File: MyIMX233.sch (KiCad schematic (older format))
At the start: 81 parts, among them IC1 iMX233, IC2 DDR_SDRAM_MT46_x16, J1 USB_OTG, P1 4p2, P2 1v2, P3 VDDA1v8, P4 2v5, P5 3v3, P6 1v, SW1 SWITCH_PUSHBUTTON, Y1 24Mhz

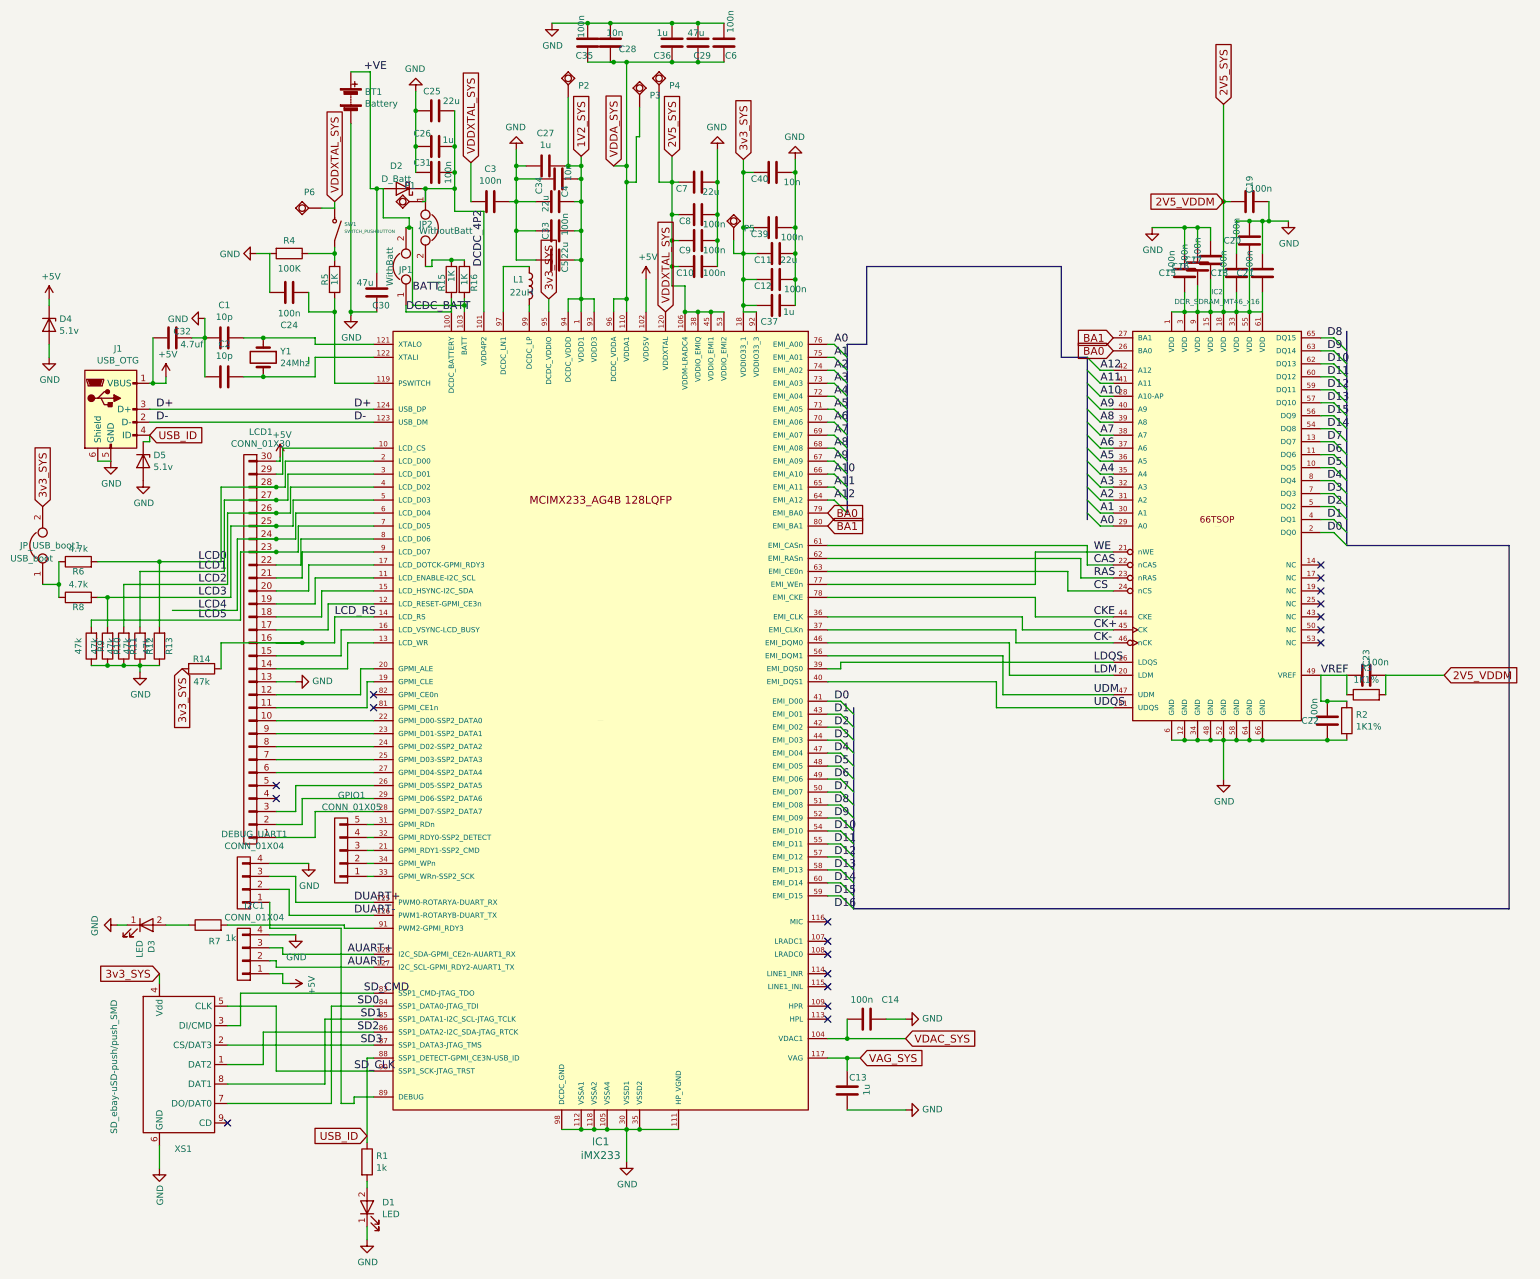
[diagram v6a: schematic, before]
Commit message: added electrolytic caps and fixed a bug in RAM CS and CE resistors
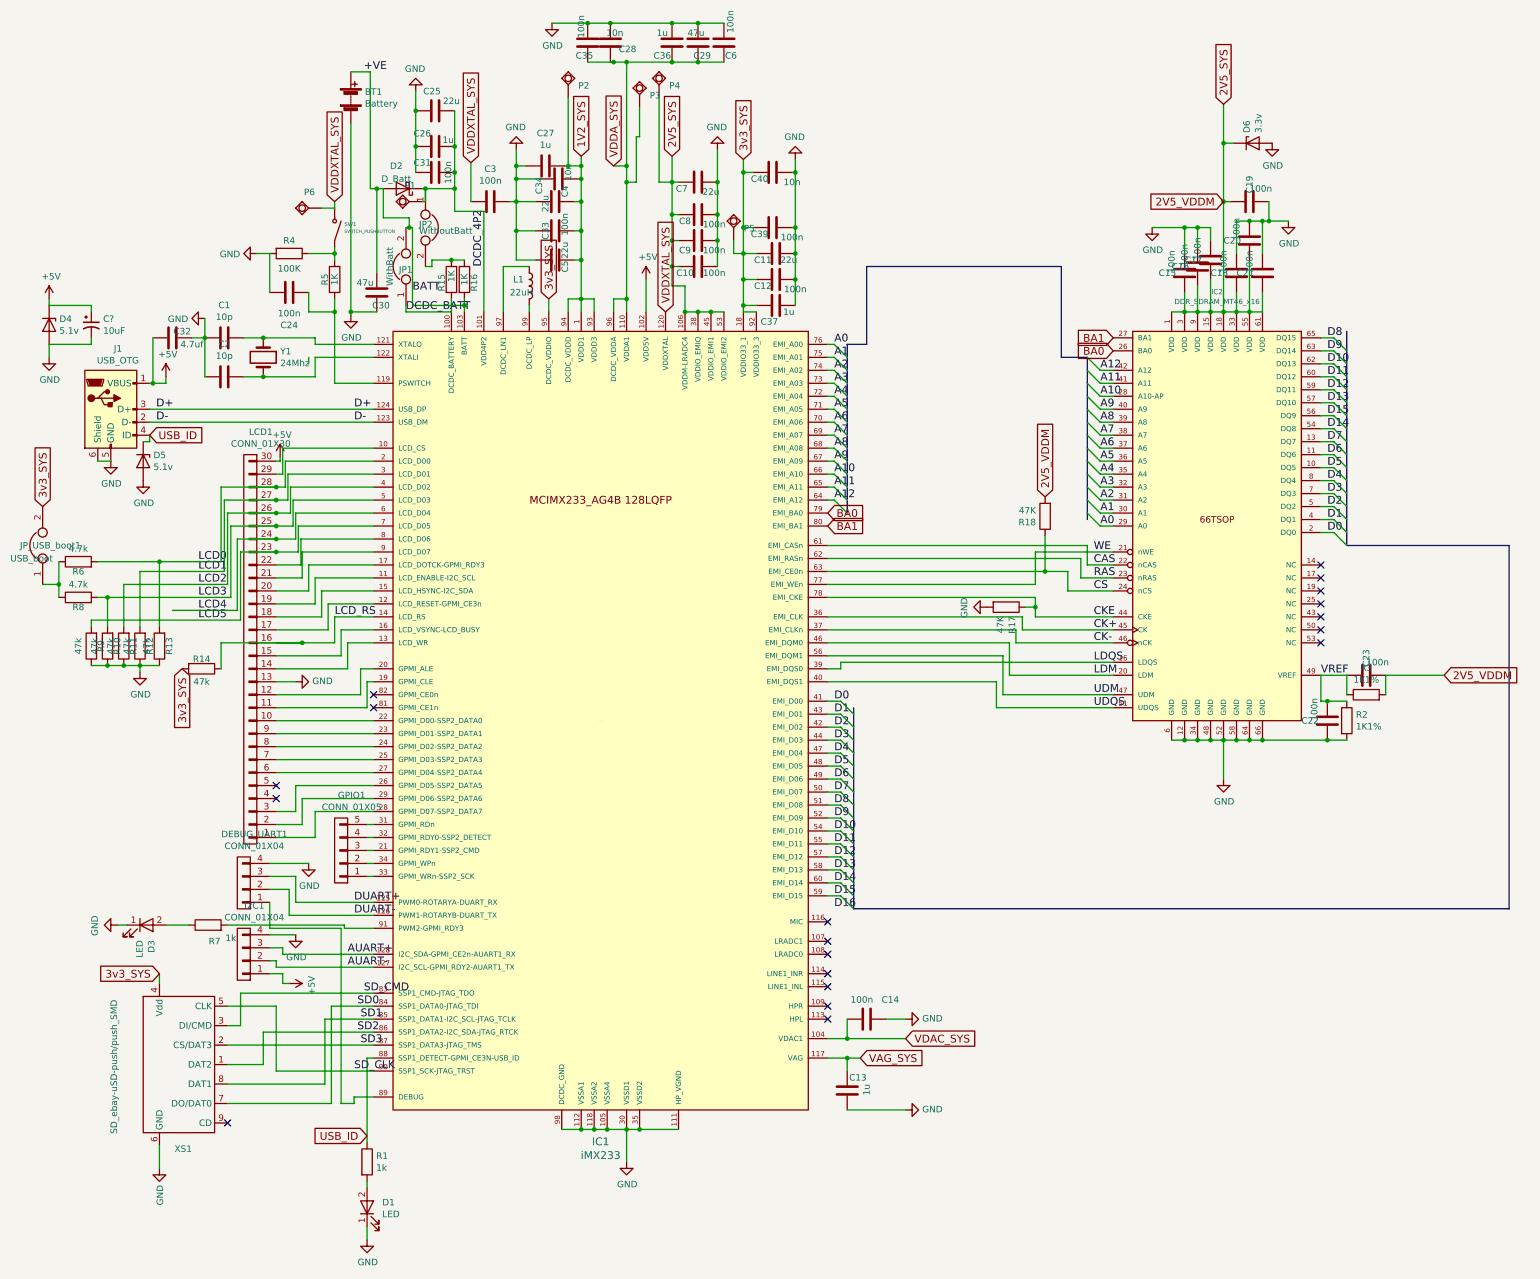
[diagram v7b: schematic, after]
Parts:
- added C?: 10uF, symbol CP1_Small
- added D6: 3.3v, Diodes_SMD:D_SOD-123, symbol D_Zener
- added R17, R18: 47K, Resistors_SMD:R_0603, symbol R
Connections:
- net +5V: now also C?.1
- net 2V5_SYS: now also D6.1 (K), R18.2
- net CKE: now also R17.1
- net CS: now also R18.1
- net GND: now also C?.2, D6.2 (A), R17.2
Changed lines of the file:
@@
 Wire Wire Line
 	1125 3900 1225 3900
+$Comp
+L R R17
+U 1 1 599BFE1C
+P 8125 5025
+F 0 "R17" H 8195 5071 50  0000 L CNN
+F 1 "47K" H 8195 4980 50  0000 L CNN
+F 2 "Resistors_SMD:R_0603" V 8055 5025 50  0001 C CNN
+F 3 "" H 8125 5025 50  0001 C CNN
+	1    8125 5025
+	0    1    1    0
+$EndComp
+$Comp
+L GND #PWR030
+U 1 1 599C0215
+P 7975 5025
+F 0 "#PWR030" H 7975 4775 50  0001 C CNN
+F 1 "GND" H 7980 4852 50  0000 C CNN
+F 2 "" H 7975 5025 50  0001 C CNN
+F 3 "" H 7975 5025 50  0001 C CNN
+	1    7975 5025
+	0    1    1    0
+$EndComp
+Wire Wire Line
+	8275 5025 8350 5025
+Connection ~ 8350 5025
+$Comp
+L R R18
+U 1 1 599C06F3
+P 8425 4325
+F 0 "R18" H 8495 4371 50  0000 L CNN
+F 1 "47K" H 8495 4280 50  0000 L CNN
+F 2 "Resistors_SMD:R_0603" V 8355 4325 50  0001 C CNN
+F 3 "" H 8425 4325 50  0001 C CNN
+	1    8425 4325
+	-1   0    0    1
+$EndComp
+Wire Wire Line
+	8425 4475 8425 4750
+Connection ~ 8425 4750
+Text GLabel 8425 4175 1    60   Input ~ 0
+2V5_VDDM
+$Comp
+L D_Zener D6
+U 1 1 599C640F
+P 10025 1450
+F 0 "D6" V 9979 1529 50  0000 L CNN
+F 1 "3.3v" V 10070 1529 50  0000 L CNN
+F 2 "Diodes_SMD:D_SOD-123" H 10025 1450 50  0001 C CNN
+F 3 "" H 10025 1450 50  0001 C CNN
+	1    10025 1450
+	1    0    0    -1
+$EndComp
+Wire Wire Line
+	9875 1450 9800 1450
+Connection ~ 9800 1450
+$Comp
+L GND #PWR031
+U 1 1 599C703F
+P 10175 1450
+F 0 "#PWR031" H 10175 1200 50  0001 C CNN
+F 1 "GND" H 10180 1277 50  0000 C CNN
+F 2 "" H 10175 1450 50  0001 C CNN
+F 3 "" H 10175 1450 50  0001 C CNN
+	1    10175 1450
+	1    0    0    -1
+$EndComp
+$Comp
+L CP1_Small C?
+U 1 1 599CB281
+P 1075 2850
+F 0 "C?" H 1166 2896 50  0000 L CNN
+F 1 "10uF" H 1166 2805 50  0000 L CNN
+F 2 "" H 1075 2850 50  0001 C CNN
+F 3 "" H 1075 2850 50  0001 C CNN
+	1    1075 2850
+	1    0    0    -1
+$EndComp
+Wire Wire Line
+	1075 2750 1075 2700
+Wire Wire Line
+	1075 2700 750  2700
+Wire Wire Line
+	1075 2950 1075 3000
+Wire Wire Line
+	1075 3000 750  3000
 $EndSCHEMATC

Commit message: squashed 5 commits
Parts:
- added C41: 1u, Capacitors_SMD:C_0603_HandSoldering, symbol C
- added D10: 5.1v, Diodes_SMD:D_SOD-323_HandSoldering, symbol D_Zener
- added D7, D9: 5.1v, Diodes_THT:D_DO-35_SOD27_P7.62mm_Horizontal, symbol D_Zener
- added D8: 3.3v, Diodes_THT:D_DO-35_SOD27_P7.62mm_Horizontal, symbol D_Zener
- added R19: 0.1ohm, Resistors_SMD:R_0603_HandSoldering, symbol R
- C38: renamed from C?; footprint (none) -> Capacitors_THT:CP_Radial_D5.0mm_P2.50mm
- C7: value 22u -> 1u
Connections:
- net +5V: now also D7.1 (K), R19.2; no longer C38.1
- net +VE: now also D10.1 (K)
- net 2V5_SYS: now also D8.1 (K)
- net DCDC_BATT: now also C41.2
- net GND: now also C41.1, D10.2 (A), D7.2 (A), D8.2 (A), D9.2 (A)
- net USB_ID: now also D9.1 (K)
- new net: C38.1, R19.1
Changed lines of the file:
@@
 P 5750 1750
 F 0 "C7" V 5800 1625 50  0000 C CNN
-F 1 "22u" V 5825 1850 50  0000 C CNN
+F 1 "1u" V 5825 1850 50  0000 C CNN
 F 2 "Capacitors_SMD:C_0805_HandSoldering" H 5788 1600 50  0001 C CNN
 F 3 "" H 5750 1750 50  0001 C CNN
@@
 	3225 900  3225 1800
 Wire Wire Line
-	3225 1800 3325 1800
+	3150 1800 3325 1800
 Wire Wire Line
 	3075 1300 3075 2775
@@
 Connection ~ 2500 4600
 Wire Wire Line
-	1525 3750 1525 3700
+	1525 3700 1525 3775
 Wire Wire Line
 	1475 3750 1525 3750
@@
 	3550 2700 3950 2700
 Wire Wire Line
-	3500 2700 3500 2750
-Wire Wire Line
-	3500 2750 3850 2750
+	3500 2700 3500 2800
+Wire Wire Line
+	3850 2750 3500 2750
 Wire Wire Line
 	3525 2025 3525 2100
@@
 $EndComp
 $Comp
-L CP1_Small C?
+L CP1_Small C38
 U 1 1 599CB281
 P 1075 2850
-F 0 "C?" H 1166 2896 50  0000 L CNN
+F 0 "C38" H 1166 2896 50  0000 L CNN
 F 1 "10uF" H 1166 2805 50  0000 L CNN
-F 2 "" H 1075 2850 50  0001 C CNN
+F 2 "Capacitors_THT:CP_Radial_D5.0mm_P2.50mm" H 1075 2850 50  0001 C CNN
 F 3 "" H 1075 2850 50  0001 C CNN
 	1    1075 2850
@@
 $EndComp
 Wire Wire Line
-	1075 2750 1075 2700
-Wire Wire Line
-	1075 2700 750  2700
-Wire Wire Line
-	1075 2950 1075 3000
-Wire Wire Line
-	1075 3000 750  3000
+	1075 2700 1075 2750
+Wire Wire Line
+	1075 3000 1075 2950
+Wire Wire Line
+	600  3000 1075 3000
+$Comp
+L D_Zener D7
+U 1 1 59A32633
+P 600 2850
+F 0 "D7" V 554 2929 50  0000 L CNN
+F 1 "5.1v" V 645 2929 50  0000 L CNN
+F 2 "Diodes_THT:D_DO-35_SOD27_P7.62mm_Horizontal" H 600 2850 50  0001 C CNN
+F 3 "" H 600 2850 50  0001 C CNN
+	1    600  2850
+	0    1    1    0
+$EndComp
+Connection ~ 750  2700
+Connection ~ 750  3000
+$Comp
+L C C41
+U 1 1 59A33BBD
+P 3350 2800
+F 0 "C41" V 3225 2850 50  0000 C CNN
+F 1 "1u" V 3300 2700 50  0000 C CNN
+F 2 "Capacitors_SMD:C_0603_HandSoldering" H 3388 2650 50  0001 C CNN
+F 3 "" H 3350 2800 50  0001 C CNN
+	1    3350 2800
+	0    -1   -1   0
+$EndComp
+Wire Wire Line
+	3200 2800 3200 2750
+Connection ~ 3200 2750
+Connection ~ 3500 2750
+$Comp
+L R R19
+U 1 1 59A35CB7
+P 925 2700
+F 0 "R19" V 825 2675 50  0000 C CNN
+F 1 "0.1ohm" V 850 2875 50  0000 C CNN
+F 2 "Resistors_SMD:R_0603_HandSoldering" V 855 2700 50  0001 C CNN
+F 3 "" H 925 2700 50  0001 C CNN
+	1    925  2700
+	0    1    1    0
+$EndComp
+Wire Wire Line
+	600  2700 775  2700
+$Comp
+L D_Zener D8
+U 1 1 59A38647
+P 10000 1200
+F 0 "D8" V 9954 1279 50  0000 L CNN
+F 1 "3.3v" V 10045 1279 50  0000 L CNN
+F 2 "Diodes_THT:D_DO-35_SOD27_P7.62mm_Horizontal" H 10000 1200 50  0001 C CNN
+F 3 "" H 10000 1200 50  0001 C CNN
+	1    10000 1200
+	1    0    0    -1
+$EndComp
+Wire Wire Line
+	9850 1200 9800 1200
+Connection ~ 9800 1200
+Wire Wire Line
+	10150 1200 10175 1200
+Wire Wire Line
+	10175 1200 10175 1450
+$Comp
+L D_Zener D9
+U 1 1 59A3E765
+P 1675 3925
+F 0 "D9" V 1629 4004 50  0000 L CNN
+F 1 "5.1v" V 1720 4004 50  0000 L CNN
+F 2 "Diodes_THT:D_DO-35_SOD27_P7.62mm_Horizontal" H 1675 3925 50  0001 C CNN
+F 3 "" H 1675 3925 50  0001 C CNN
+	1    1675 3925
+	0    1    1    0
+$EndComp
+Wire Wire Line
+	1525 3775 1675 3775
+Connection ~ 1525 3750
+Wire Wire Line
+	1675 4075 1575 4075
+Wire Wire Line
+	1575 4075 1575 4050
+Wire Wire Line
+	1575 4050 1475 4050
+$Comp
+L D_Zener D10
+U 1 1 59A40581
+P 3150 2150
+F 0 "D10" V 3104 2229 50  0000 L CNN
+F 1 "5.1v" V 3195 2229 50  0000 L CNN
+F 2 "Diodes_SMD:D_SOD-323_HandSoldering" H 3150 2150 50  0001 C CNN
+F 3 "" H 3150 2150 50  0001 C CNN
+	1    3150 2150
+	0    1    1    0
+$EndComp
+Wire Wire Line
+	3150 2000 3150 1800
+Connection ~ 3225 1800
+Wire Wire Line
+	3150 2300 3150 2750
+Connection ~ 3150 2750
 $EndSCHEMATC
